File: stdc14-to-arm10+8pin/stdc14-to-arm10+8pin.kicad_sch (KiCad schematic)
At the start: 3 parts, among them J1 Conn_ARM_JTAG_SWD_10, J2 Conn_ST_STDC14, J3 Conn_02x04_Counter_Clockwise

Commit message: prob fin?
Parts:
- added H1, H2: MountingHole_Pad, MountingHole:MountingHole_2.7mm_M2.5_Pad, symbol Mechanical:MountingHole_Pad
- added TP1: SWDIO, TestPoint:TestPoint_Pad_D1.0mm, symbol Connector:TestPoint
- added TP2: SWO, TestPoint:TestPoint_Pad_D1.0mm, symbol Connector:TestPoint
- added TP3: SWCLK, TestPoint:TestPoint_Pad_D1.0mm, symbol Connector:TestPoint
- added TP4: NRST, TestPoint:TestPoint_Pad_D1.0mm, symbol Connector:TestPoint
- added TP5: VCC, TestPoint:TestPoint_Pad_D1.0mm, symbol Connector:TestPoint
- added TP6: GND, TestPoint:TestPoint_Pad_D1.0mm, symbol Connector:TestPoint
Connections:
- net GND: now also H1.1, H2.1, TP6.1
- net NRST: now also TP4.1
- net SWCLK: now also TP3.1
- net SWDIO: now also TP1.1
- net SWO: now also TP2.1
- net VCC: now also TP5.1
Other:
- moved on the sheet: J1, J2, J3

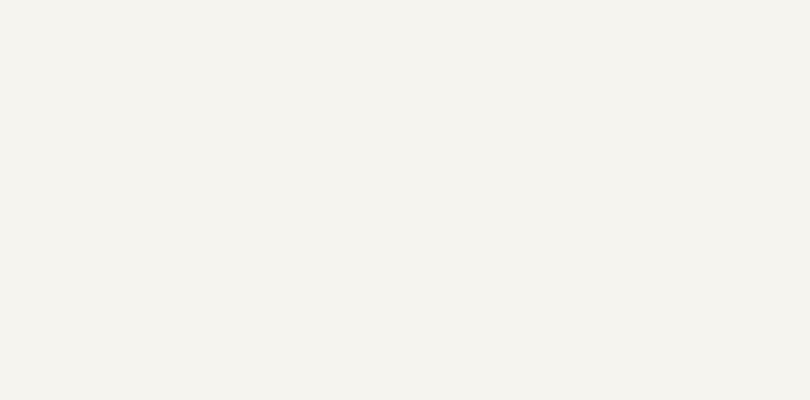
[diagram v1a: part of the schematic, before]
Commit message: moved some traces, add decoupling
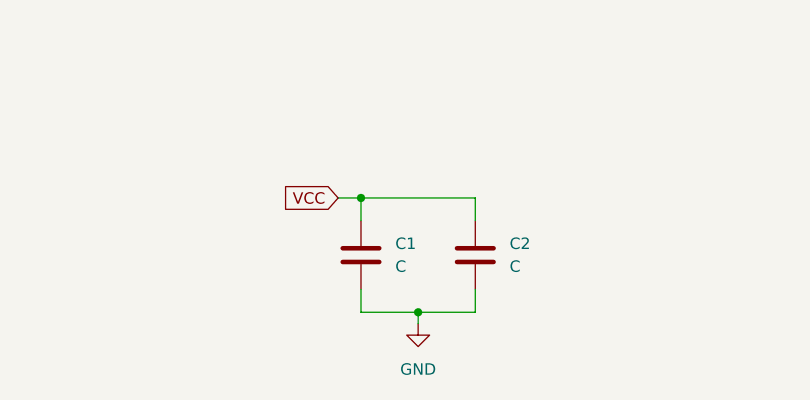
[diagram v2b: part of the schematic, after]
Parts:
- added C1, C2: C, Capacitor_SMD:C_0805_2012Metric, symbol Device:C
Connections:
- net GND: now also C1.2, C2.2
- net VCC: now also C1.1, C2.1
